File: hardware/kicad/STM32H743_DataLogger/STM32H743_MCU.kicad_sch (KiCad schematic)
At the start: 41 parts, among them J10 SWD Debug, J11 USB-C, J12 UART Debug Console, J13 BOOT0 Select, J14 TC2050-IDC SWD, U10 STM32H743VIT6, Y1 25MHz, Y2 32.768kHz

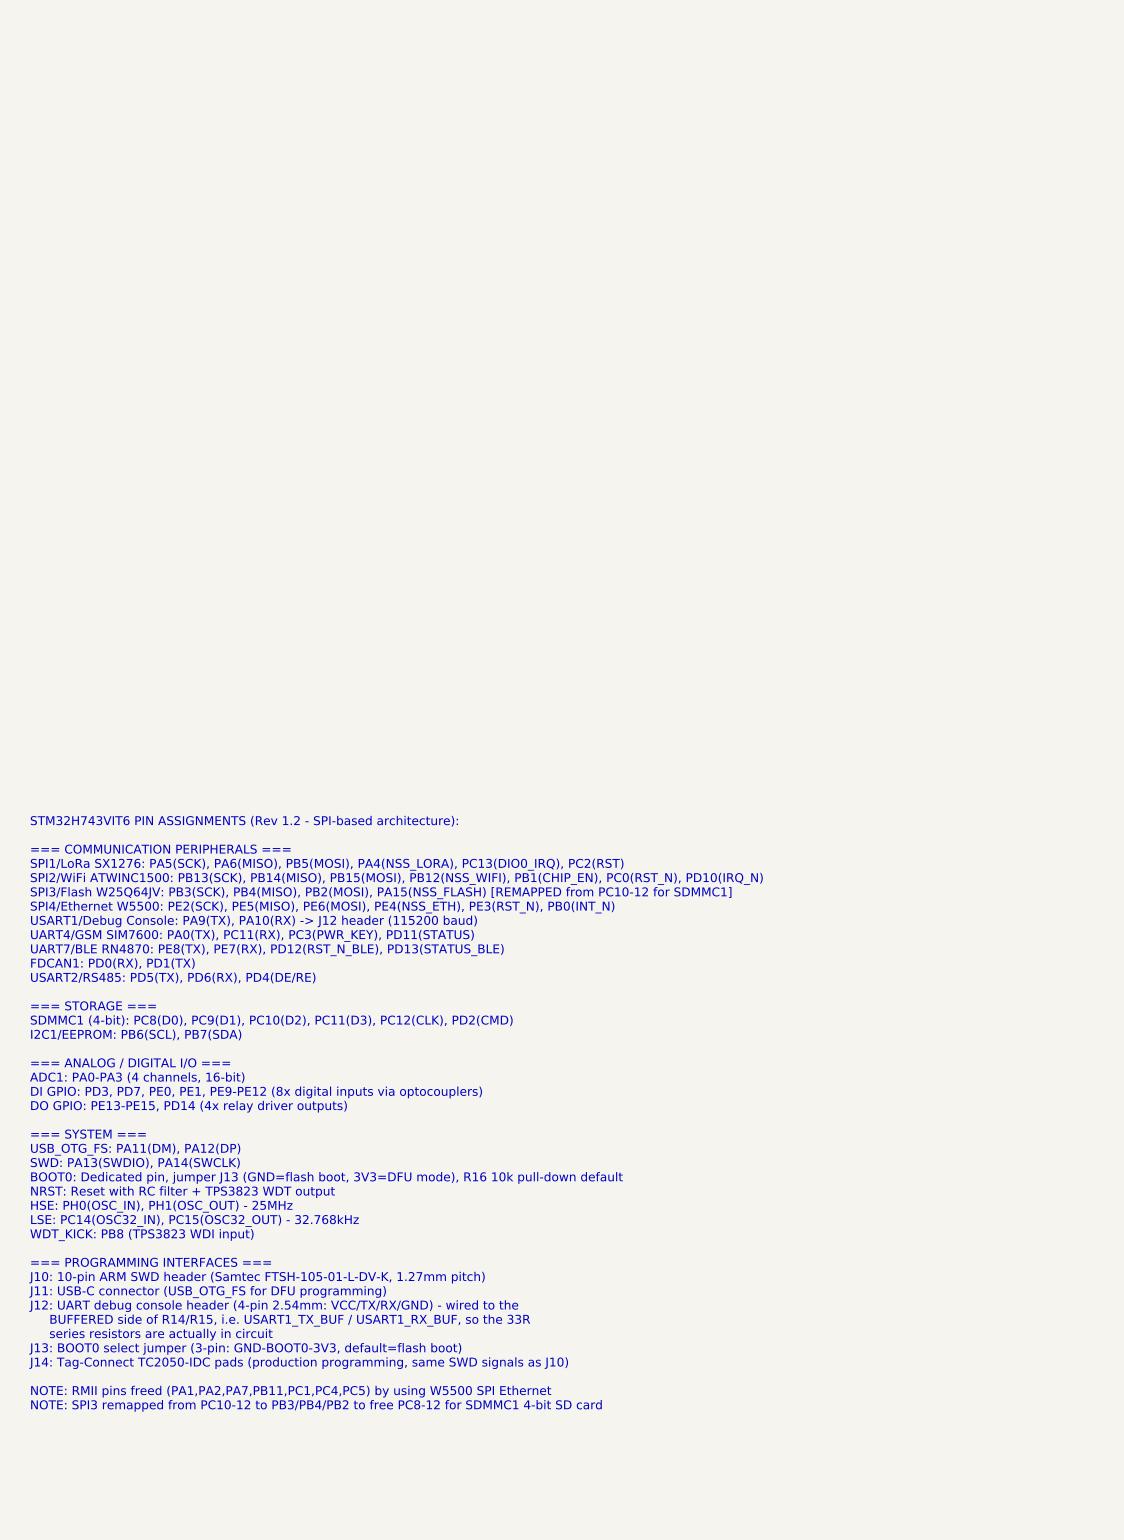
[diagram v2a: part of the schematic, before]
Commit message: Rebuild the MCU pin assignment from the real LQFP-100 pinout
With KiCad available I could fetch the MCU_ST_STM32H7 symbol library,
which carries the STM32H743VITx pin table generated from the ST datasheet
— the authoritative source that was missing when I flagged this as
blocking. U10's pad-to-net map is rebuilt from it.

Verified against the pins the package fixes, all of which now land
correctly: NRST=14, BOOT0=94, VBAT=6, VDDA/VREF+/VSSA=21/20/19,
VCAP=48/73, VDD=11/27/50/75/100, VSS=10/26/49/74/99. +24V no longer
appears anywhere on the MCU. 90 pins assigned, 10 left spare.

The symbol also carries per-pin alternate-function lists, which resolved
the two conflicts the old notes contained without guesswork:

- UART4_TX moves PA0 -> PB9. PA0 is an ADC1 channel and the four analog
  inputs must stay on PA0-PA3; PB9 was the only free UART4_TX-capable pin.
- UART4_RX moves PC11 -> PB8. PC11 is SDMMC1_D3, and all five
  UART4_RX-capable pins were occupied, so WDT_KICK gave up PB8.
- WDT_KICK moves PB8 -> PD9, displaced by the above. It only drives the
  TPS3823 watchdog input, so any free GPIO serves.
- LORA_RST and GSM_PWR_KEY move off PC2/PC3 to PB10/PB11: on the 100-pin
  package those are the dual-pad PC2_C/PC3_C direct-analog variants, and
  both signals are plain GPIO resets that should not depend on the analog
  switch.

SD_CD was never assigned in the old notes at all; it is now on PD15.

These four reassignments change the firmware pin map and need sign-off.
They are recorded in design spec 7.8 and in the MCU sheet annotation,
which now carries the full signal-to-pin table instead of port names.

All 157 nets still reach at least two pads. The DO NOT FABRICATE banner
is removed. The old routing was cut for the previous pinout and has been
discarded; re-routing is in progress.

Co-Authored-By: Claude Opus 5 <noreply@anthropic.com>
Claude-Session: https://claude.ai/code/session_01XsiZ6LJT6X46LKY8yEbRbx
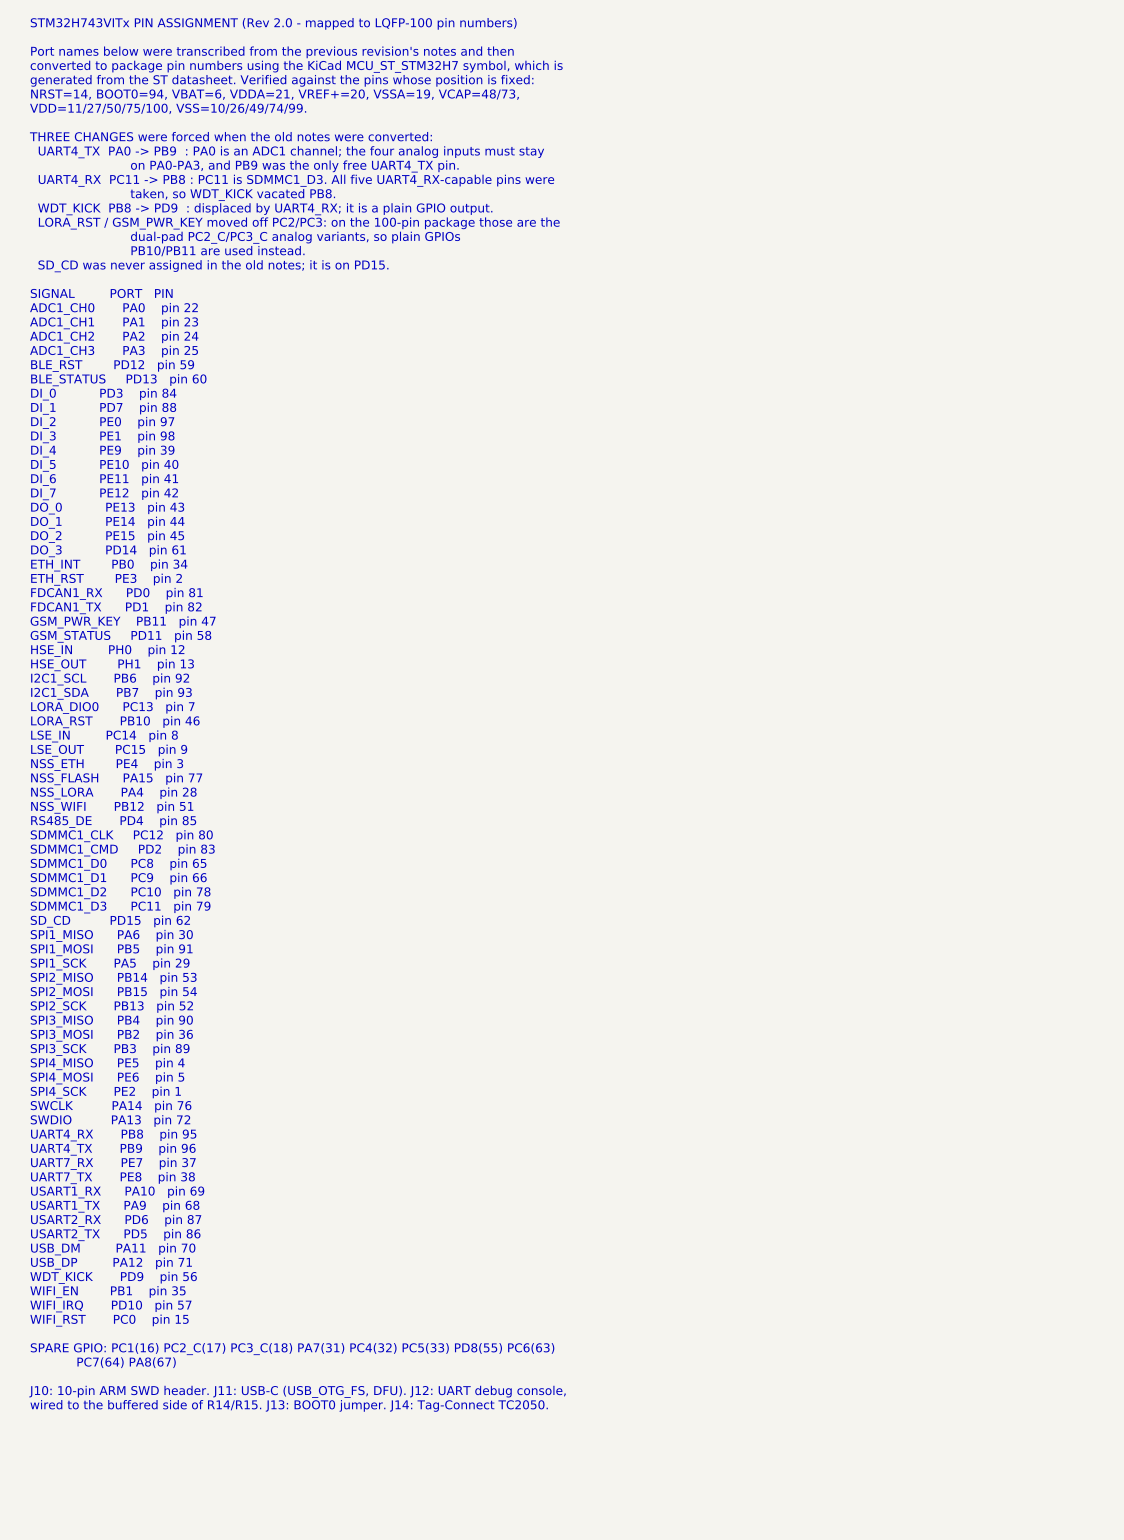
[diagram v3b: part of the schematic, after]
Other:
- note added: "STM32H743VITx PIN ASSIGNMENT (Rev 2.0 - mapped to LQFP-100 pin numbers) Port names below were transcribed from the previous revision's notes and then converted to package pin numbers using the KiCad MCU_ST_STM32H7 symbol, which is generated from the ST datasheet. Verified against the pins whose position is fixed: NRST=14, BOOT0=94, VBAT=6, VDDA=21, VREF+=20, VSSA=19, VCAP=48/73, VDD=11/27/50/75/1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"
- note removed: "STM32H743VIT6 PIN ASSIGNMENTS (Rev 1.2 - SPI-based architecture): === COMMUNICATION PERIPHERALS === SPI1/LoRa SX1276: PA5(SCK), PA6(MISO), PB5(MOSI), PA4(NSS_LORA), PC13(DIO0_IRQ), PC2(RST) SPI2/WiFi ATWINC1500: PB13(SCK), PB14(MISO), PB15(MOSI), PB12(NSS_WIFI), PB1(CHIP_EN), PC0(RST_N), PD10(IRQ_N) SPI3/Flash W25Q64JV: PB3(SCK), PB4(MISO), PB2(MOSI), PA15(NSS_FLASH) [REMAPPED from PC10-12 for SD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"
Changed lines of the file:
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@@
   ;; PIN ASSIGNMENTS (documented as text annotation)
   ;; ============================================================
-  (text "STM32H743VIT6 PIN ASSIGNMENTS (Rev 1.2 - SPI-based architecture):\n\n=== COMMUNICATION PERIPHERALS ===\nSPI1/LoRa SX1276: PA5(SCK), PA6(MISO), PB5(MOSI), PA4(NSS_LORA), PC13(DIO0_IRQ), PC2(RST)\nSPI2/WiFi ATWINC1500: PB13(SCK), PB14(MISO), PB15(MOSI), PB12(NSS_WIFI), PB1(CHIP_EN), PC0(RST_N), PD10(IRQ_N)\nSPI3/Flash W25Q64JV: PB3(SCK), PB4(MISO), PB2(MOSI), PA15(NSS_FLASH) [REMAPPED from PC10-12 for SDMMC1]\nSPI4/Ethernet W5500: PE2(SCK), PE5(MISO), PE6(MOSI), PE4(NSS_ETH), PE3(RST_N), PB0(INT_N)\nUSART1/Debug Console: PA9(TX), PA10(RX) -> J12 header (115200 baud)\nUART4/GSM SIM7600: PA0(TX), PC11(RX), PC3(PWR_KEY), PD11(STATUS)\nUART7/BLE RN4870: PE8(TX), PE7(RX), PD12(RST_N_BLE), PD13(STATUS_BLE)\nFDCAN1: PD0(RX), PD1(TX)\nUSART2/RS485: PD5(TX), PD6(RX), PD4(DE/RE)\n\n=== STORAGE ===\nSDMMC1 (4-bit): PC8(D0), PC9(D1), PC10(D2), PC11(D3), PC12(CLK), PD2(CMD)\nI2C1/EEPROM: PB6(SCL), PB7(SDA)\n\n=== ANALOG / DIGITAL I/O ===\nADC1: PA0-PA3 (4 channels, 16-bit)\nDI GPIO: PD3, PD7, PE0, PE1, PE9-PE12 (8x digital inputs via optocouplers)\nDO GPIO: PE13-PE15, PD14 (4x relay driver outputs)\n\n=== SYSTEM ===\nUSB_OTG_FS: PA11(DM), PA12(DP)\nSWD: PA13(SWDIO), PA14(SWCLK)\nBOOT0: Dedicated pin, jumper J13 (GND=flash boot, 3V3=DFU mode), R16 10k pull-down default\nNRST: Reset with RC filter + TPS3823 WDT output\nHSE: PH0(OSC_IN), PH1(OSC_OUT) - 25MHz\nLSE: PC14(OSC32_IN), PC15(OSC32_OUT) - 32.768kHz\nWDT_KICK: PB8 (TPS3823 WDI input)\n\n=== PROGRAMMING INTERFACES ===\nJ10: 10-pin ARM SWD header (Samtec FTSH-105-01-L-DV-K, 1.27mm pitch)\nJ11: USB-C connector (USB_OTG_FS for DFU programming)\nJ12: UART debug console header (4-pin 2.54mm: VCC/TX/RX/GND) - wired to the\n     BUFFERED side of R14/R15, i.e. USART1_TX_BUF / USART1_RX_BUF, so the 33R\n     series resistors are actually in circuit\nJ13: BOOT0 select jumper (3-pin: GND-BOOT0-3V3, default=flash boot)\nJ14: Tag-Connect TC2050-IDC pads (production programming, same SWD signals as J10)\n\nNOTE: RMII pins freed (PA1,PA2,PA7,PB11,PC1,PC4,PC5) by using W5500 SPI Ethernet\nNOTE: SPI3 remapped from PC10-12 to PB3/PB4/PB2 to free PC8-12 for SDMMC1 4-bit SD card"
+  (text "STM32H743VITx PIN ASSIGNMENT (Rev 2.0 - mapped to LQFP-100 pin numbers)\n\nPort names below were transcribed from the previous revision's notes and then\nconverted to package pin numbers using the KiCad MCU_ST_STM32H7 symbol, which is\ngenerated from the ST datasheet. Verified against the pins whose position is fixed:\nNRST=14, BOOT0=94, VBAT=6, VDDA=21, VREF+=20, VSSA=19, VCAP=48/73,\nVDD=11/27/50/75/100, VSS=10/26/49/74/99.\n\nTHREE CHANGES were forced when the old notes were converted:\n  UART4_TX  PA0 -> PB9  : PA0 is an ADC1 channel; the four analog inputs must stay\n                          on PA0-PA3, and PB9 was the only free UART4_TX pin.\n  UART4_RX  PC11 -> PB8 : PC11 is SDMMC1_D3. All five UART4_RX-capable pins were\n                          taken, so WDT_KICK vacated PB8.\n  WDT_KICK  PB8 -> PD9  : displaced by UART4_RX; it is a plain GPIO output.\n  LORA_RST / GSM_PWR_KEY moved off PC2/PC3: on the 100-pin package those are the\n                          dual-pad PC2_C/PC3_C analog variants, so plain GPIOs\n                          PB10/PB11 are used instead.\n  SD_CD was never assigned in the old notes; it is on PD15.\n\nSIGNAL         PORT   PIN\nADC1_CH0       PA0    pin 22\nADC1_CH1       PA1    pin 23\nADC1_CH2       PA2    pin 24\nADC1_CH3       PA3    pin 25\nBLE_RST        PD12   pin 59\nBLE_STATUS     PD13   pin 60\nDI_0           PD3    pin 84\nDI_1           PD7    pin 88\nDI_2           PE0    pin 97\nDI_3           PE1    pin 98\nDI_4           PE9    pin 39\nDI_5           PE10   pin 40\nDI_6           PE11   pin 41\nDI_7           PE12   pin 42\nDO_0           PE13   pin 43\nDO_1           PE14   pin 44\nDO_2           PE15   pin 45\nDO_3           PD14   pin 61\nETH_INT        PB0    pin 34\nETH_RST        PE3    pin 2\nFDCAN1_RX      PD0    pin 81\nFDCAN1_TX      PD1    pin 82\nGSM_PWR_KEY    PB11   pin 47\nGSM_STATUS     PD11   pin 58\nHSE_IN         PH0    pin 12\nHSE_OUT        PH1    pin 13\nI2C1_SCL       PB6    pin 92\nI2C1_SDA       PB7    pin 93\nLORA_DIO0      PC13   pin 7\nLORA_RST       PB10   pin 46\nLSE_IN         PC14   pin 8\nLSE_OUT        PC15   pin 9\nNSS_ETH        PE4    pin 3\nNSS_FLASH      PA15   pin 77\nNSS_LORA       PA4    pin 28\nNSS_WIFI       PB12   pin 51\nRS485_DE       PD4    pin 85\nSDMMC1_CLK     PC12   pin 80\nSDMMC1_CMD     PD2    pin 83\nSDMMC1_D0      PC8    pin 65\nSDMMC1_D1      PC9    pin 66\nSDMMC1_D2      PC10   pin 78\nSDMMC1_D3      PC11   pin 79\nSD_CD          PD15   pin 62\nSPI1_MISO      PA6    pin 30\nSPI1_MOSI      PB5    pin 91\nSPI1_SCK       PA5    pin 29\nSPI2_MISO      PB14   pin 53\nSPI2_MOSI      PB15   pin 54\nSPI2_SCK       PB13   pin 52\nSPI3_MISO      PB4    pin 90\nSPI3_MOSI      PB2    pin 36\nSPI3_SCK       PB3    pin 89\nSPI4_MISO      PE5    pin 4\nSPI4_MOSI      PE6    pin 5\nSPI4_SCK       PE2    pin 1\nSWCLK          PA14   pin 76\nSWDIO          PA13   pin 72\nUART4_RX       PB8    pin 95\nUART4_TX       PB9    pin 96\nUART7_RX       PE7    pin 37\nUART7_TX       PE8    pin 38\nUSART1_RX      PA10   pin 69\nUSART1_TX      PA9    pin 68\nUSART2_RX      PD6    pin 87\nUSART2_TX      PD5    pin 86\nUSB_DM         PA11   pin 70\nUSB_DP         PA12   pin 71\nWDT_KICK       PD9    pin 56\nWIFI_EN        PB1    pin 35\nWIFI_IRQ       PD10   pin 57\nWIFI_RST       PC0    pin 15\n\nSPARE GPIO: PC1(16) PC2_C(17) PC3_C(18) PA7(31) PC4(32) PC5(33) PD8(55) PC6(63)\n            PC7(64) PA8(67)\n\nJ10: 10-pin ARM SWD header. J11: USB-C (USB_OTG_FS, DFU). J12: UART debug console,\nwired to the buffered side of R14/R15. J13: BOOT0 jumper. J14: Tag-Connect TC2050."
     (exclude_from_sim no)
     (at 25.4 25.4 0)

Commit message: Verify every IC against its datasheet pinout; rebuild three, add missing parts
The MCU turned out not to be the only placeholder. With the symbol
libraries available I checked each IC's footprint wiring against the pin
names its datasheet-derived KiCad symbol gives — if a pin the datasheet
calls VDD is not on a supply net, the map was not derived from the
datasheet. Three ICs failed and are rebuilt:

- U50 W5500 had SPI on the Ethernet differential pins and supplies and
  grounds on ten wrong pads. Rebuilt from the 48-pin pinout: SPI on
  32-37, TX/RX pairs on 1/2/5/6, PMODE2..0 grounded for all-capable
  auto-negotiation.
- U40 ISO3082 had the receiver and driver swapped, the bus A/B pair one
  pin out, and GND2 carrying the isolated 5V supply.
- U1 TPS54560 had the switch node on pins 7 and 8, shorting SW to GND,
  and FB off pin 5.

Verifying the W5500 also showed three datasheet-required parts were never
placed: R56 (12.4k on EXRES1, sets transmit bias current), C87 (4.7uF on
TOCAP) and C88 (100nF on VBG). All three added.

Two ICs cannot be verified and are recorded as such rather than guessed
at. U60 is worse than a wiring error: the footprint is QFN-28 4x4mm on
0.4mm pitch, but SX1276IMLTRT is 6x6mm on 0.65mm pitch — the wrong
package outline entirely. U3's part is the DGN (MSOP-8-EP) variant and
the library only has KTT (TO-263-5), a different pinout, so it cannot
stand in. Six more ICs have no symbol at all and show the same sequential
pattern; they should be assumed wrong until checked.

Still open on the buck: EN, RT/CLK and COMP have no components on them.
RT/CLK sets the switching frequency and COMP is the compensation network,
so U1 will not regulate as drawn.

Also corrected twelve wrong schematic lib_ids against the real libraries;
35 of 44 now resolve, and the nine that need symbols drawn are listed in
docs/Schematic_Symbol_Audit.md.

BOM now 123 line items / 222 components; netlist 160 nets, all reaching
at least two pads.

Co-Authored-By: Claude O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
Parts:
- J11: symbol Connector:USB_C_Receptacle_USB2.0 -> Connector:USB_C_Receptacle_USB2.0_16P
- J14: symbol Connector:Tag-Connect_TC2050-IDC -> Connector:TC2050
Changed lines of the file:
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@@
   ;; ============================================================
   (symbol
-    (lib_id "Connector:USB_C_Receptacle_USB2.0")
+    (lib_id "Connector:USB_C_Receptacle_USB2.0_16P")
     (at 215.9 139.7)
     (unit 1)
@@
   ;; ============================================================
   (symbol
-    (lib_id "Connector:Tag-Connect_TC2050-IDC")
+    (lib_id "Connector:TC2050")
     (at 254.0 143.51)
     (unit 1)
